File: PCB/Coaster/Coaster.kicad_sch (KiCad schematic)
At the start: 55 parts, among them J1 Shelly, J2 USB-C, U1 ESP32-PICO-MINI-02, U2 LMR16006XDDCR, U3 QR

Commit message: Tidy
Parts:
- removed D13: LED_BARG, RevK:MHS190RGBCT, symbol Device:LED_BARG
- removed R2: 300R, RevK:R_0603, symbol Device:R
- removed R3: 1K, RevK:R_0603, symbol Device:R
- removed R4: 100R, RevK:R_0603, symbol Device:R
- added C?: C, symbol Device:C
- added J1: Join, RevK:PCB-Join, symbol Mechanical:MountingHole
- added Logo1: AJK, RevK:AJK, symbol RevK:AJK
- D9: LCSC Part # C4154881 -> C114586
- H1, H10, H11, H12, H2, H3, H4, H5, H6, H7, H8, H9: now left out of the parts list
- renumbered J1 to J2, J2 to J3
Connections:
- net GND: now also C?.1
- net B: no longer names the net of U1.35 (IO21)
- net EN: no longer names the net of R1.2, U1.8 (EN)
- net EN: now also C?.2
- net G: no longer names the net of U1.28 (IO8)
- net R: no longer names the net of U1.26 (IO20)
- no-connect marks 22 -> 25
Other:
- moved on the sheet: R1

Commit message: Tracked
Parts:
- removed C?: C, symbol Device:C
- added C16: 10nF, Capacitor_SMD:C_0603_1608Metric, symbol Device:C
- added P1, P10, P11, P12, P13, P2, P3, P4, P5, P6, P7, P8, P9: TestPoint, RevK:PAD, symbol Connector:TestPoint
- added T1, T10, T11, T12, T13, T2, T3, T4, T5, T6, T7, T8, T9: TestPoint, RevK:PAD-LINK, symbol Connector:TestPoint
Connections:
- net +3V3: now also P11.1; no longer J2.3 (3V3)
- net GND: now also C16.1, P5.1, P6.1, P7.1, P8.1; no longer C1.2, C10.2, C11.2, C12.2, C2.2, C3.2, C4.2, C5.2, C6.2, C7.2, C8.2, C9.2, D1.3 (VSS), D10.3 (VSS), D11.3 (VSS), D12.3 (VSS), D2.3 (VSS), D3.3 (VSS), D4.3 (VSS), D5.3 (VSS), D6.3 (VSS), D7.3 (VSS), D8.3 (VSS), D9.3 (VSS), J2.1 (GND), J3.A1 (GND), J3.A12 (GND), J3.B1 (GND), J3.B12 (GND), J3.S1 (SHIELD)
- net GPIO0: now also T12.1; no longer U1.23 (IO0)
- net I: now also T10.1; no longer U1.30 (RXD0)
- net LED: now also T13.1; no longer U1.34 (IO22)
- net O: now also T9.1; no longer U1.31 (TXD0)
- net VBUS: now also P1.1, P2.1; no longer C1.1, C10.1, C11.1, C12.1, C2.1, C3.1, C4.1, C5.1, C6.1, C7.1, C8.1, C9.1, D1.1 (VDD), D10.1 (VDD), D11.1 (VDD), D12.1 (VDD), D2.1 (VDD), D3.1 (VDD), D4.1 (VDD), D5.1 (VDD), D6.1 (VDD), D7.1 (VDD), D8.1 (VDD), D9.1 (VDD), J3.A4 (VBUS), J3.A9 (VBUS), J3.B4 (VBUS), J3.B9 (VBUS)
- net at R5.1: now also P3.1; no longer J3.A5 (CC1)
- net at R6.2: now also P4.1; no longer J3.B5 (CC2)
- net at R1.2, U1.8 (EN): now also C16.2
- new net: J3.A5 (CC1), T3.1
- new net: J3.B5 (CC2), T4.1
- new net: P9.1, U1.31 (TXD0)
- new net: P13.1, U1.34 (IO22)
- new net: P12.1, U1.23 (IO0)
- new net: P10.1, U1.30 (RXD0)
- new net +3.3VA: J2.3 (3V3), T11.1
- new net GND2: C1.2, C10.2, C11.2, C12.2, C2.2, C3.2, C4.2, C5.2, C6.2, C7.2, C8.2, C9.2, D1.3 (VSS), D10.3 (VSS), D11.3 (VSS), D12.3 (VSS), D2.3 (VSS), D3.3 (VSS), D4.3 (VSS), D5.3 (VSS), D6.3 (VSS), D7.3 (VSS), D8.3 (VSS), D9.3 (VSS), J2.1 (GND), J3.A1 (GND), J3.A12 (GND), J3.B1 (GND), J3.B12 (GND), J3.S1 (SHIELD), T5.1, T6.1, T7.1, T8.1
- new net VCC: C1.1, C10.1, C11.1, C12.1, C2.1, C3.1, C4.1, C5.1, C6.1, C7.1, C8.1, C9.1, D1.1 (VDD), D10.1 (VDD), D11.1 (VDD), D12.1 (VDD), D2.1 (VDD), D3.1 (VDD), D4.1 (VDD), D5.1 (VDD), D6.1 (VDD), D7.1 (VDD), D8.1 (VDD), D9.1 (VDD), J3.A4 (VBUS), J3.A9 (VBUS), J3.B4 (VBUS), J3.B9 (VBUS), T1.1, T2.1
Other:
- moved on the sheet: J2, R5, R6

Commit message: More tidy
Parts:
- added P? (x4): TestPoint, RevK:PAD, symbol Connector:TestPoint
- added T? (x4): TestPoint, RevK:PAD-LINK, symbol Connector:TestPoint
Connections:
- net GND: now also P?.1, P?.1, P?.1, P?.1
- net GND2: now also T?.1, T?.1, T?.1, T?.1

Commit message: Tidy
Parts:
- gave numbers to parts that had none: 8
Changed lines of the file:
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@@
   (symbol (lib_id "power:GND") (at 160.02 146.05 270) (mirror x) (unit 1)
     (in_bom yes) (on_board yes)
-    (property "Reference" "#PWR?" (id 0) (at 153.67 146.05 0)
+    (property "Reference" "#PWR0119" (id 0) (at 153.67 146.05 0)
       (effects (font (size 1.27 1.27)) hide)
     )
@@
   (symbol (lib_id "power:GND") (at 160.02 149.86 270) (mirror x) (unit 1)
     (in_bom yes) (on_board yes)
-    (property "Reference" "#PWR?" (id 0) (at 153.67 149.86 0)
+    (property "Reference" "#PWR0122" (id 0) (at 153.67 149.86 0)
       (effects (font (size 1.27 1.27)) hide)
     )
@@
   (symbol (lib_id "power:GND2") (at 177.8 153.67 90) (mirror x) (unit 1)
     (in_bom yes) (on_board yes)
-    (property "Reference" "#PWR?" (id 0) (at 184.15 153.67 0)
+    (property "Reference" "#PWR0125" (id 0) (at 184.15 153.67 0)
       (effects (font (size 1.27 1.27)) hide)
     )
@@
   (symbol (lib_id "power:GND") (at 160.02 142.24 270) (mirror x) (unit 1)
     (in_bom yes) (on_board yes)
-    (property "Reference" "#PWR?" (id 0) (at 153.67 142.24 0)
+    (property "Reference" "#PWR0121" (id 0) (at 153.67 142.24 0)
       (effects (font (size 1.27 1.27)) hide)
     )
@@
   (symbol (lib_id "Connector:TestPoint") (at 160.02 146.05 270) (mirror x) (unit 1)
     (in_bom no) (on_board yes)
-    (property "Reference" "P?" (id 0) (at 165.1 146.05 90)
+    (property "Reference" "P15" (id 0) (at 165.1 146.05 90)
       (effects (font (size 1.27 1.27)) (justify left))
     )
@@
   (symbol (lib_id "power:GND2") (at 177.8 149.86 90) (mirror x) (unit 1)
     (in_bom yes) (on_board yes)
-    (property "Reference" "#PWR?" (id 0) (at 184.15 149.86 0)
+    (property "Reference" "#PWR0126" (id 0) (at 184.15 149.86 0)
       (effects (font (size 1.27 1.27)) hide)
     )
@@
   (symbol (lib_id "power:GND") (at 160.02 153.67 270) (mirror x) (unit 1)
     (in_bom yes) (on_board yes)
-    (property "Reference" "#PWR?" (id 0) (at 153.67 153.67 0)
+    (property "Reference" "#PWR0120" (id 0) (at 153.67 153.67 0)
       (effects (font (size 1.27 1.27)) hide)
     )
@@
   (symbol (lib_id "Connector:TestPoint") (at 177.8 149.86 90) (mirror x) (unit 1)
     (in_bom no) (on_board yes)
-    (property "Reference" "T?" (id 0) (at 172.72 149.86 90)
+    (property "Reference" "T16" (id 0) (at 172.72 149.86 90)
       (effects (font (size 1.27 1.27)) (justify left))
     )
@@
   (symbol (lib_id "Connector:TestPoint") (at 177.8 142.24 90) (mirror x) (unit 1)
     (in_bom no) (on_board yes)
-    (property "Reference" "T?" (id 0) (at 172.72 142.24 90)
+    (property "Reference" "T14" (id 0) (at 172.72 142.24 90)
       (effects (font (size 1.27 1.27)) (justify left))
     )
@@
   (symbol (lib_id "power:GND2") (at 177.8 142.24 90) (mirror x) (unit 1)
     (in_bom yes) (on_board yes)
-    (property "Reference" "#PWR?" (id 0) (at 184.15 142.24 0)
+    (property "Reference" "#PWR0123" (id 0) (at 184.15 142.24 0)
       (effects (font (size 1.27 1.27)) hide)
     )
@@
   (symbol (lib_id "Connector:TestPoint") (at 177.8 153.67 90) (mirror x) (unit 1)
     (in_bom no) (on_board yes)
-    (property "Reference" "T?" (id 0) (at 172.72 153.67 90)
+    (property "Reference" "T17" (id 0) (at 172.72 153.67 90)
       (effects (font (size 1.27 1.27)) (justify left))
     )
@@
   (symbol (lib_id "power:GND2") (at 177.8 146.05 90) (mirror x) (unit 1)
     (in_bom yes) (on_board yes)
-    (property "Reference" "#PWR?" (id 0) (at 184.15 146.05 0)
+    (property "Reference" "#PWR0124" (id 0) (at 184.15 146.05 0)
       (effects (font (size 1.27 1.27)) hide)
     )
@@
   (symbol (lib_id "Connector:TestPoint") (at 160.02 149.86 270) (mirror x) (unit 1)
     (in_bom no) (on_board yes)
-    (property "Reference" "P?" (id 0) (at 165.1 149.86 90)
+    (property "Reference" "P16" (id 0) (at 165.1 149.86 90)
       (effects (font (size 1.27 1.27)) (justify left))
     )
@@
   (symbol (lib_id "Connector:TestPoint") (at 160.02 142.24 270) (mirror x) (unit 1)
     (in_bom no) (on_board yes)
-    (property "Reference" "P?" (id 0) (at 165.1 142.24 90)
+    (property "Reference" "P14" (id 0) (at 165.1 142.24 90)
       (effects (font (size 1.27 1.27)) (justify left))
     )
@@
   (symbol (lib_id "Connector:TestPoint") (at 177.8 146.05 90) (mirror x) (unit 1)
     (in_bom no) (on_board yes)
-    (property "Reference" "T?" (id 0) (at 172.72 146.05 90)
+    (property "Reference" "T15" (id 0) (at 172.72 146.05 90)
       (effects (font (size 1.27 1.27)) (justify left))
     )
@@
   (symbol (lib_id "Connector:TestPoint") (at 160.02 153.67 270) (mirror x) (unit 1)
     (in_bom no) (on_board yes)
-    (property "Reference" "P?" (id 0) (at 165.1 153.67 90)
+    (property "Reference" "P17" (id 0) (at 165.1 153.67 90)
       (effects (font (size 1.27 1.27)) (justify left))
     )
@@
     )
     (path "/077aeece-90ee-45dc-903a-8fe281e5a53c"
-      (reference "#PWR?") (unit 1) (value "GND") (footprint "")
+      (reference "#PWR0119") (unit 1) (value "GND") (footprint "")
+    )
+    (path "/7230ae76-35ac-4173-bdc6-e1e76b3d19b4"
+      (reference "#PWR0120") (unit 1) (value "GND") (footprint "")
+    )
+    (path "/30ef273a-c7f1-400d-a809-3c83efb09136"
+      (reference "#PWR0121") (unit 1) (value "GND") (footprint "")
     )
     (path "/0ba7056c-2c55-4233-b7b4-f969b54f174a"
-      (reference "#PWR?") (unit 1) (value "GND") (footprint "")
+      (reference "#PWR0122") (unit 1) (value "GND") (footprint "")
+    )
+    (path "/a07ba548-438d-4931-840b-126d5da147e7"
+      (reference "#PWR0123") (unit 1) (value "GND2") (footprint "")
+    )
+    (path "/b90d6ac4-cd4a-4bb0-b040-a39295528cde"
+      (reference "#PWR0124") (unit 1) (value "GND2") (footprint "")
     )
     (path "/16834351-e3db-40ae-834b-fcc308a697f1"
-      (reference "#PWR?") (unit 1) (value "GND2") (footprint "")
-    )
-    (path "/30ef273a-c7f1-400d-a809-3c83efb09136"
-      (reference "#PWR?") (unit 1) (value "GND") (footprint "")
+      (reference "#PWR0125") (unit 1) (value "GND2") (footprint "")
     )
     (path "/452a0754-1d5b-45ab-bcbe-38ccf6eeab3d"
-      (reference "#PWR?") (unit 1) (value "GND2") (footprint "")
-    )
-    (path "/7230ae76-35ac-4173-bdc6-e1e76b3d19b4"
-      (reference "#PWR?") (unit 1) (value "GND") (footprint "")
-    )
-    (path "/a07ba548-438d-4931-840b-126d5da147e7"
-      (reference "#PWR?") (unit 1) (value "GND2") (footprint "")
-    )
-    (path "/b90d6ac4-cd4a-4bb0-b040-a39295528cde"
-      (reference "#PWR?") (unit 1) (value "GND2") (footprint "")
+      (reference "#PWR0126") (unit 1) (value "GND2") (footprint "")
     )
     (path "/e86cc638-a81f-4cb4-8994-a8593b7c68f7"
@@
       (reference "P13") (unit 1) (value "TestPoint") (footprint "RevK:PAD")
     )
+    (path "/df493c42-d8bc-40f4-81f5-b929eb9163b3"
+      (reference "P14") (unit 1) (value "TestPoint") (footprint "RevK:PAD")
+    )
     (path "/382c6bbb-fb1a-44f9-9858-69b2d74b1ae6"
-      (reference "P?") (unit 1) (value "TestPoint") (footprint "RevK:PAD")
+      (reference "P15") (unit 1) (value "TestPoint") (footprint "RevK:PAD")
     )
     (path "/bcaee71a-fc72-4d59-86ac-7b8cf30b9a0a"
-      (reference "P?") (unit 1) (value "TestPoint") (footprint "RevK:PAD")
-    )
-    (path "/df493c42-d8bc-40f4-81f5-b929eb9163b3"
-      (reference "P?") (unit 1) (value "TestPoint") (footprint "RevK:PAD")
+      (reference "P16") (unit 1) (value "TestPoint") (footprint "RevK:PAD")
     )
     (path "/fe8c4bbf-14fa-410c-84d6-8d3881a53ab7"
-      (reference "P?") (unit 1) (value "TestPoint") (footprint "RevK:PAD")
+      (reference "P17") (unit 1) (value "TestPoint") (footprint "RevK:PAD")
     )
     (path "/3b6e2e43-685e-4e7b-97b9-8f290ca51417"
@@
       (reference "T13") (unit 1) (value "TestPoint") (footprint "RevK:PAD-LINK")
     )
+    (path "/8378ecbf-b20f-4bf3-860f-2eb5b09bdcda"
+      (reference "T14") (unit 1) (value "TestPoint") (footprint "RevK:PAD-LINK")
+    )
+    (path "/e05172ae-ada1-48da-8329-b6cceb7f7713"
+      (reference "T15") (unit 1) (value "TestPoint") (footprint "RevK:PAD-LINK")
+    )
     (path "/7d5b4a89-2067-4503-a23f-bff88787fe94"
-      (reference "T?") (unit 1) (value "TestPoint") (footprint "RevK:PAD-LINK")
-    )
-    (path "/8378ecbf-b20f-4bf3-860f-2eb5b09bdcda"
-      (reference "T?") (unit 1) (value "TestPoint") (footprint "RevK:PAD-LINK")
+      (reference "T16") (unit 1) (value "TestPoint") (footprint "RevK:PAD-LINK")
     )
     (path "/b37e1a0b-361f-48fd-b6a3-05a4d4d437c5"
-      (reference "T?") (unit 1) (value "TestPoint") (footprint "RevK:PAD-LINK")
-    )
-    (path "/e05172ae-ada1-48da-8329-b6cceb7f7713"
-      (reference "T?") (unit 1) (value "TestPoint") (footprint "RevK:PAD-LINK")
+      (reference "T17") (unit 1) (value "TestPoint") (footprint "RevK:PAD-LINK")
     )
     (path "/7943a3d5-b195-4a57-b3e1-ee29355f1eeb"

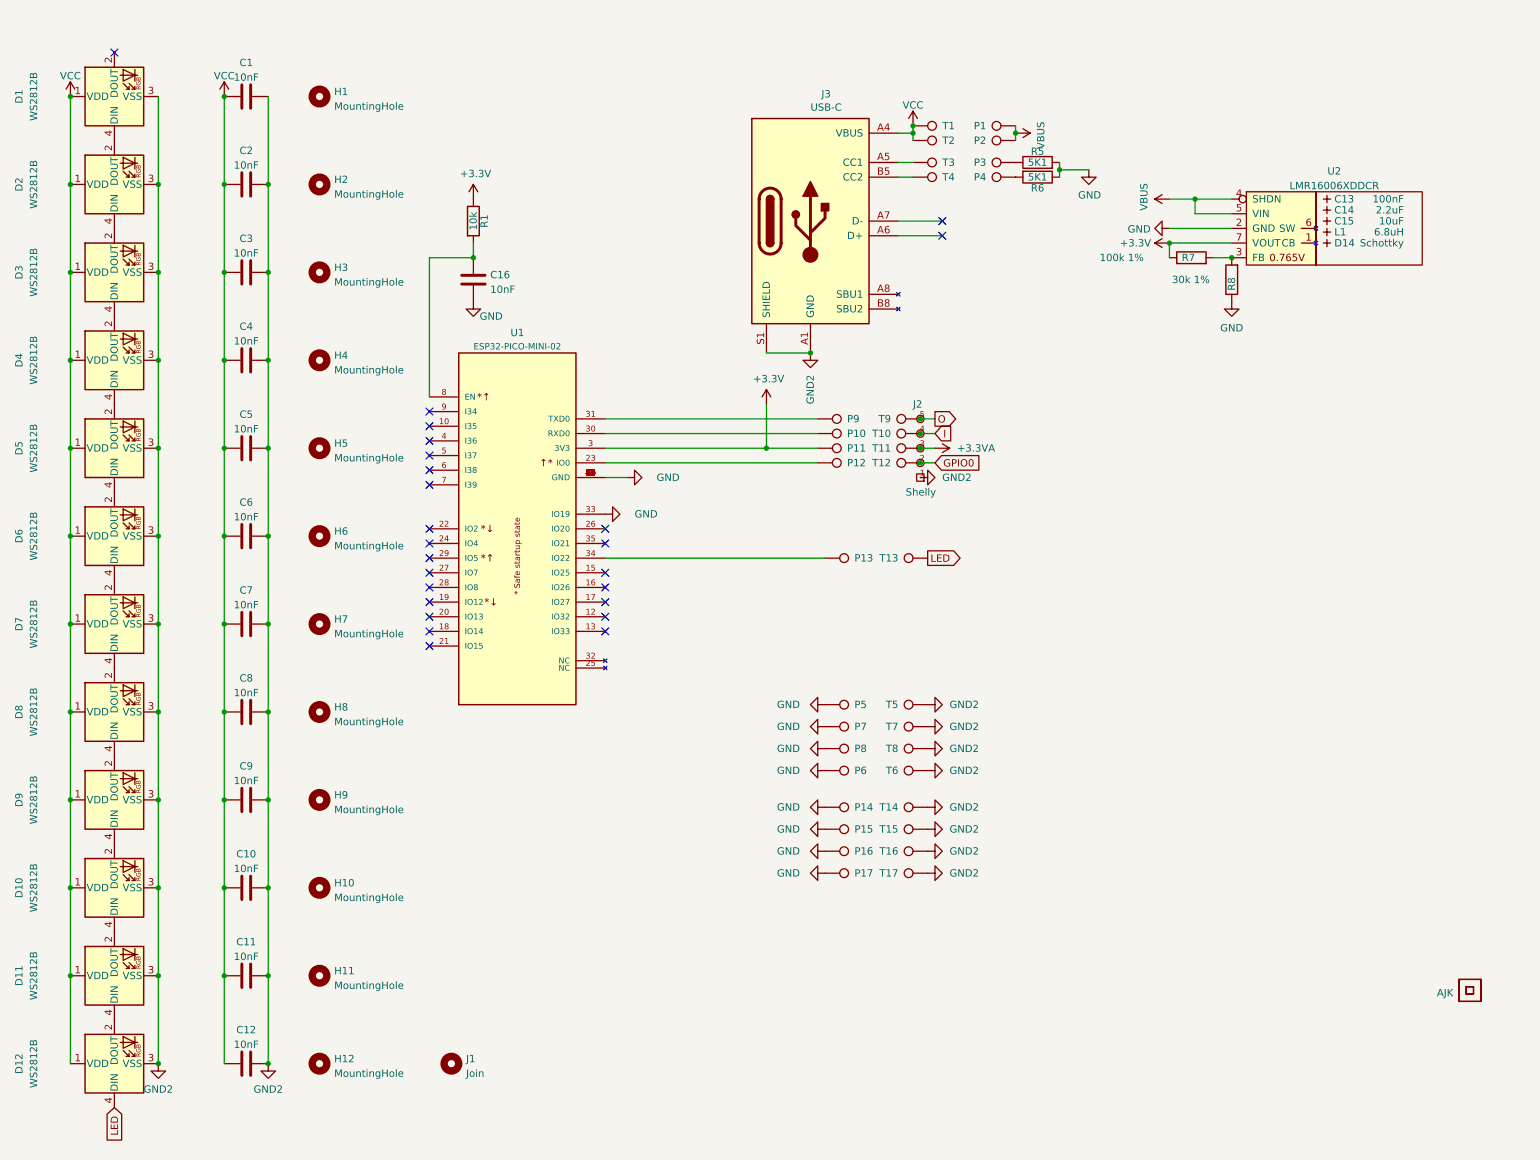
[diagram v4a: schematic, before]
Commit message: Reworked for rubber feet
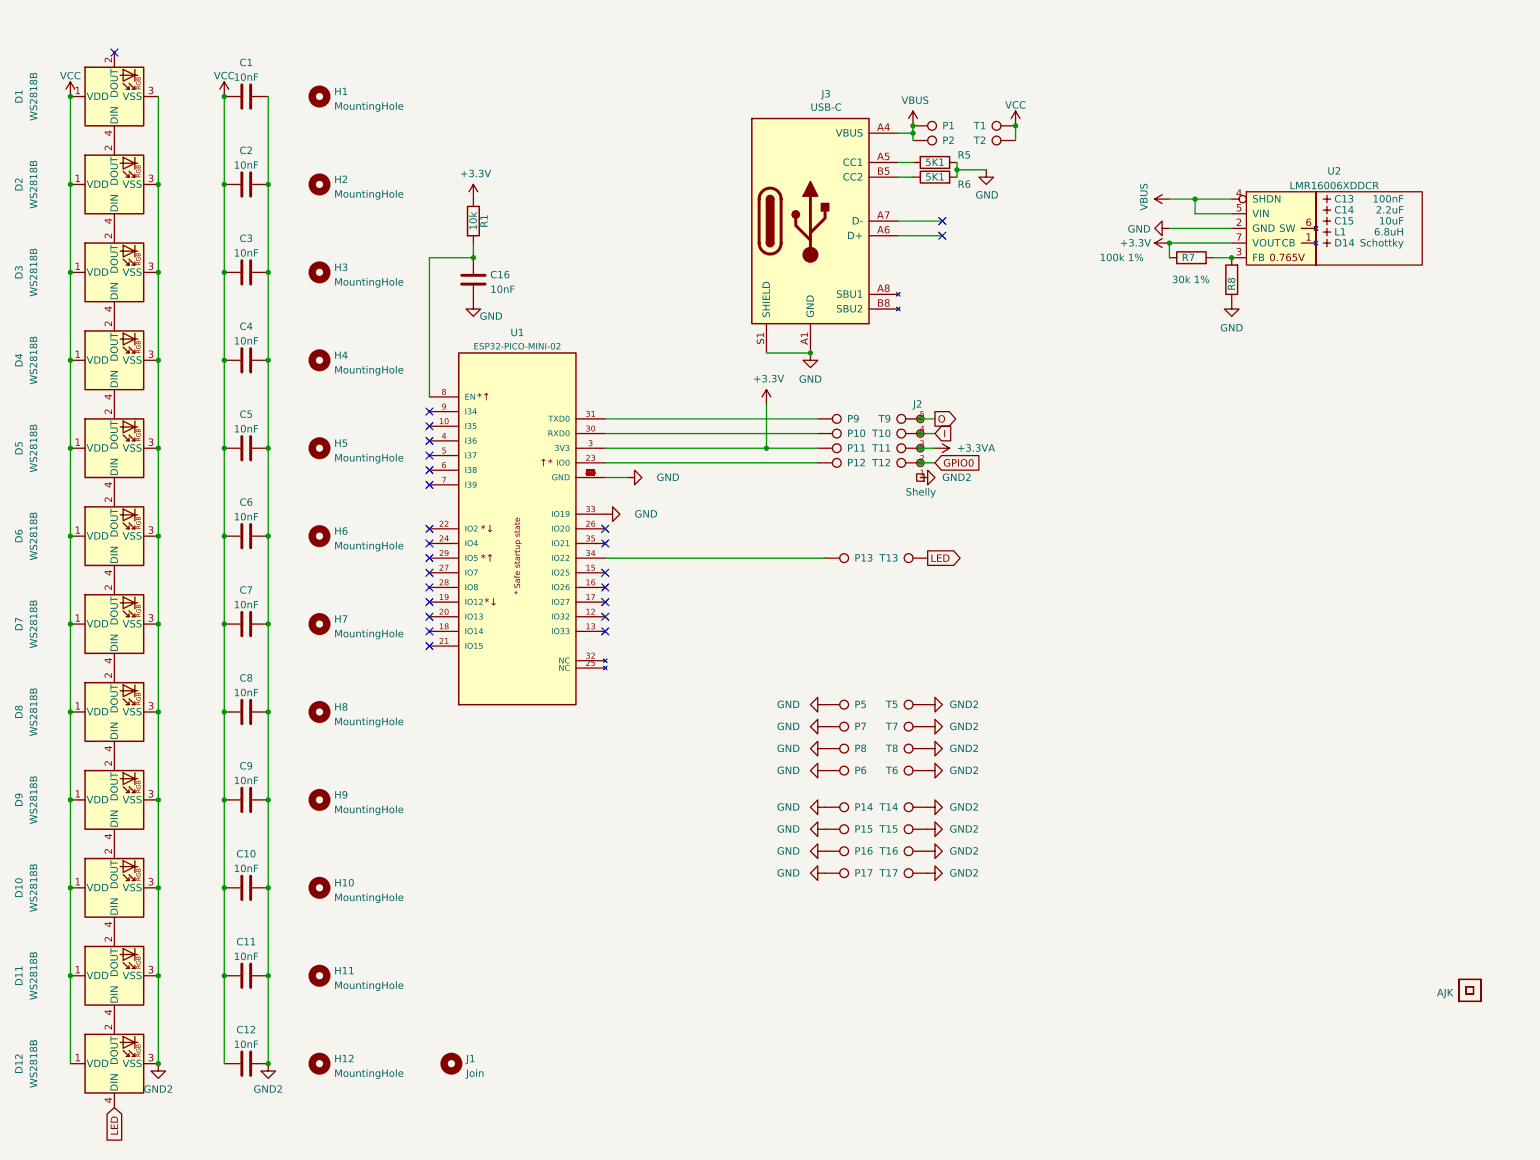
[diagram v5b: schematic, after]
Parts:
- removed P3, P4: TestPoint, RevK:PAD, symbol Connector:TestPoint
- removed T3, T4: TestPoint, RevK:PAD-LINK, symbol Connector:TestPoint
- D1, D10, D11, D12, D2, D3, D4, D5, D6, D7, D8: value WS2812B -> WS2818B; footprint LED_SMD:LED_WS2812B_PLCC4_5.0x5.0mm_P3.2mm -> RevK:SMD5050; LCSC Part # C4154881 -> C114586
- D9: value WS2812B -> WS2818B; footprint LED_SMD:LED_WS2812B_PLCC4_5.0x5.0mm_P3.2mm -> RevK:SMD5050
- J1: now left out of the parts list
- J3: JLCPCB Rotation Offset 180 -> (none)
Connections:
- net GND: now also J3.A1 (GND), J3.A12 (GND), J3.B1 (GND), J3.B12 (GND), J3.S1 (SHIELD)
- net GND2: no longer J3.A1 (GND), J3.A12 (GND), J3.B1 (GND), J3.B12 (GND), J3.S1 (SHIELD)
- net VBUS: now also J3.A4 (VBUS), J3.A9 (VBUS), J3.B4 (VBUS), J3.B9 (VBUS)
- net VCC: no longer J3.A4 (VBUS), J3.A9 (VBUS), J3.B4 (VBUS), J3.B9 (VBUS)
- net at R5.1: now also J3.B5 (CC2)
- net at R6.2: now also J3.A5 (CC1)
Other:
- moved on the sheet: P1, P2, R5, R6, T1, T2

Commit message: Much tidying
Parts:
- removed P14, P15, P16, P17: TestPoint, RevK:PAD, symbol Connector:TestPoint
- removed T14, T15, T16, T17: TestPoint, RevK:PAD-LINK, symbol Connector:TestPoint
- added C13, C14, C15, C16, C17, C18, C19, C20, C21, C22, C23, C24, C25, C26, C27, C28, C29, C30, C31, C32, C33, C34, C35, C36, C37, C38, C39, C40, C41, C42, C43, C44, C45, C46, C47, C48: 10nF, RevK:C_0603, symbol Device:C
- added D13, D14, D15, D16, D17, D18, D19, D20, D21, D22, D23, D24: WS2818B, RevK:SMD2020, symbol LED:WS2812B
- added H13, H14, H15, H16, H17, H18, H19, H20, H21, H22, H23, H24: MountingHole, RevK:LEDHOLE, symbol Mechanical:MountingHole
- added P12: TestPoint, RevK:PAD, symbol Connector:TestPoint
- added T12: TestPoint, RevK:PAD-LINK, symbol Connector:TestPoint
- D1, D10, D11, D12, D2, D3, D4, D5, D6, D7, D8, D9: footprint RevK:SMD5050 -> RevK:SMD2020; LCSC Part # C114586 -> C784564
- renumbered C16 to C49, C13 to C50, C14 to C51, C15 to C52, D14 to D25, J3 to J1, J1 to J3, P8 to P10, P6 to P11, P9 to P3, P10 to P4, P11 to P5, P12 to P6, P13 to P7, P5 to P8, P7 to P9, R6 to R2, R5 to R3, R7 to R4, R8 to R5, T8 to T10, T6 to T11, T9 to T3, T10 to T4, T11 to T5, T12 to T6, T13 to T7, T5 to T8, T7 to T9
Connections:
- net GND: now also P12.1
- net GND2: now also C13.2, C14.2, C15.2, C16.2, C17.2, C18.2, C19.2, C20.2, C21.2, C22.2, C23.2, C24.2, C25.2, C26.2, C27.2, C28.2, C29.2, C30.2, C31.2, C32.2, C33.2, C34.2, C35.2, C36.2, C37.2, C38.2, C39.2, C40.2, C41.2, C42.2, C43.2, C44.2, C45.2, C46.2, C47.2, C48.2, D13.3 (VSS), D14.3 (VSS), D15.3 (VSS), D16.3 (VSS), D17.3 (VSS), D18.3 (VSS), D19.3 (VSS), D20.3 (VSS), D21.3 (VSS), D22.3 (VSS), D23.3 (VSS), D24.3 (VSS), T12.1
- net LED: now also D1.4 (DIN); no longer D12.4 (DIN)
- net VCC: now also C13.1, C14.1, C15.1, C16.1, C17.1, C18.1, C19.1, C20.1, C21.1, C22.1, C23.1, C24.1, C25.1, C26.1, C27.1, C28.1, C29.1, C30.1, C31.1, C32.1, C33.1, C34.1, C35.1, C36.1, C37.1, C38.1, C39.1, C40.1, C41.1, C42.1, C43.1, C44.1, C45.1, C46.1, C47.1, C48.1, D13.1 (VDD), D14.1 (VDD), D15.1 (VDD), D16.1 (VDD), D17.1 (VDD), D18.1 (VDD), D19.1 (VDD), D20.1 (VDD), D21.1 (VDD), D22.1 (VDD), D23.1 (VDD), D24.1 (VDD)
- net at D1.2 (DOUT): now also D2.4 (DIN)
- net at D2.2 (DOUT): now also D3.4 (DIN); no longer D1.4 (DIN)
- net at D11.4 (DIN): now also D10.2 (DOUT); no longer D12.2 (DOUT)
- net at D11.2 (DOUT): now also D12.4 (DIN); no longer D10.4 (DIN)
- net at D4.2 (DOUT): now also D5.4 (DIN); no longer D3.4 (DIN)
- net at D4.4 (DIN): now also D3.2 (DOUT); no longer D5.2 (DOUT)
- net at D8.4 (DIN): now also D7.2 (DOUT); no longer D9.2 (DOUT)
- net at D9.4 (DIN): now also D8.2 (DOUT); no longer D10.2 (DOUT)
- net at D6.2 (DOUT): now also D7.4 (DIN); no longer D5.4 (DIN)
- net at D6.4 (DIN): now also D5.2 (DOUT); no longer D7.2 (DOUT)
- new net: D15.2 (DOUT), D16.4 (DIN)
- new net: D14.2 (DOUT), D15.4 (DIN)
- new net: D23.2 (DOUT), D24.4 (DIN)
- new net: D12.2 (DOUT), D13.4 (DIN)
- new net: D20.2 (DOUT), D21.4 (DIN)
- new net: D19.2 (DOUT), D20.4 (DIN)
- new net: D13.2 (DOUT), D14.4 (DIN)
- new net: D16.2 (DOUT), D17.4 (DIN)
- new net: D18.2 (DOUT), D19.4 (DIN)
- new net: D17.2 (DOUT), D18.4 (DIN)
- new net: D10.4 (DIN), D9.2 (DOUT)
- new net: D21.2 (DOUT), D22.4 (DIN)
- new net: D22.2 (DOUT), D23.4 (DIN)
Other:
- moved on the sheet: C1, C10, C11, C12, C2, C3, C4, C49, C5, C50, C51, C52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
